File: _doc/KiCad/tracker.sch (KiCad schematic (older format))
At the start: 14 parts

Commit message: Doc
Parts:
- removed Q?: 2N3906, Package_TO_SOT_THT:TO-92_Inline, symbol Transistor_BJT:2N3906
- added Q?: AO3401A, Package_TO_SOT_SMD:SOT-23, symbol Transistor_FET:AO3401A
- D? (x2): value D -> 1N5819
- R?: value 330 -> 10k
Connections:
- net labels removed: GND
- wire segments 43 -> 46
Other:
- moved on the sheet: BT?, C?, D?, J?, R?, U?

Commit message: Doc: schematic
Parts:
- R?: value 3k3 -> 6k8
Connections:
- net at U?.~ (VB): now also D?.1 (K)
- net at U?.~ (VCC): no longer U?.~ (VB)
- net at U?.~ (VB), U?.~ (VCC): now also D?.1 (K)
- new net: U?.~ (VB), U?.~ (VCC) (x4)
- now unconnected: U?.~ (VCC)
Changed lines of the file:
@@
 U 1 1 5FBB3C61
 P 5000 3550
-F 0 "U?" H 5000 4765 50  0000 C CNN
+F 0 "U?" H 5000 4765 50  0001 C CNN
 F 1 "STM32F401 BlackPill" H 5000 4674 50  0000 C CNN
 F 2 "" H 5100 4650 50  0001 C CNN
@@
 U 1 1 5FBB5448
 P 7100 3750
-F 0 "U?" H 7378 3796 50  0000 L CNN
-F 1 "SIM800L" H 7378 3705 50  0000 L CNN
+F 0 "U?" H 7378 3796 50  0001 L CNN
+F 1 "SIM800L" H 7400 3750 50  0000 L CNN
 F 2 "" H 7100 4150 50  0001 C CNN
 F 3 "" H 7100 4150 50  0001 C CNN
@@
 U 1 1 5FBC7BFE
 P 5600 2850
-F 0 "R?" H 5450 2800 50  0000 C CNN
-F 1 "3k3" H 5450 2900 50  0000 C CNN
+F 0 "R?" H 5450 2800 50  0001 C CNN
+F 1 "6k8" H 5450 2850 50  0000 C CNN
 F 2 "" V 5530 2850 50  0001 C CNN
 F 3 "~" H 5600 2850 50  0001 C CNN
@@
 U 1 1 5FBC947C
 P 6300 4650
-F 0 "C?" H 6550 4700 50  0000 C CNN
+F 0 "C?" H 6550 4700 50  0001 C CNN
 F 1 "470mF" H 6550 4600 50  0000 C CNN
 F 2 "" H 6338 4500 50  0001 C CNN
@@
 U 1 1 5FBCCE2D
 P 3650 3850
-F 0 "U?" H 3650 3500 50  0000 C CNN
-F 1 "OLED_SSD1306" H 3650 3400 50  0000 C CNN
+F 0 "U?" H 3650 3500 50  0001 C CNN
+F 1 "OLED_SSD1306" H 3650 3450 50  0000 C CNN
 F 2 "" H 3650 4250 50  0001 C CNN
 F 3 "" H 3650 4250 50  0001 C CNN
@@
 	4150 3400 4150 3800
 Connection ~ 4150 3800
-$Comp
-L Device:R R?
-U 1 1 5FBD5AD0
-P 6350 3450
-F 0 "R?" H 6420 3496 50  0000 L CNN
-F 1 "10" H 6420 3405 50  0000 L CNN
-F 2 "" V 6280 3450 50  0001 C CNN
-F 3 "~" H 6350 3450 50  0001 C CNN
-	1    6350 3450
-	1    0    0    -1
-$EndComp
 Wire Wire Line
 	4150 4400 4150 4800
@@
 U 1 1 5FBD92D9
 P 5750 4700
-F 0 "BT?" H 6000 4800 50  0000 C CNN
+F 0 "BT?" H 6000 4800 50  0001 C CNN
 F 1 "250mAh" H 6000 4700 50  0000 C CNN
 F 2 "" V 5750 4760 50  0001 C CNN
@@
 U 1 1 5FC2FAC7
 P 5850 3100
-F 0 "D?" H 5700 2950 50  0000 C CNN
-F 1 "LED" H 5700 2850 50  0000 C CNN
+F 0 "D?" H 5700 2950 50  0001 C CNN
+F 1 "LED" H 5700 2900 50  0000 C CNN
 F 2 "" H 5850 3100 50  0001 C CNN
 F 3 "~" H 5850 3100 50  0001 C CNN
@@
 U 1 1 5FBC87D2
 P 5600 4250
-F 0 "R?" H 5750 4300 50  0000 C CNN
-F 1 "10k" H 5750 4200 50  0000 C CNN
+F 0 "R?" H 5750 4300 50  0001 C CNN
+F 1 "10k" H 5750 4250 50  0000 C CNN
 F 2 "" V 5530 4250 50  0001 C CNN
 F 3 "~" H 5600 4250 50  0001 C CNN
@@
 U 1 1 5FC34600
 P 6600 2850
-F 0 "D?" V 6554 2930 50  0000 L CNN
-F 1 "1N5819" V 6645 2930 50  0000 L CNN
+F 0 "D?" V 6554 2930 50  0001 L CNN
+F 1 "1N5819" V 6600 2950 50  0000 L CNN
 F 2 "" H 6600 2850 50  0001 C CNN
 F 3 "~" H 6600 2850 50  0001 C CNN
@@
 U 1 1 5FC1A3F2
 P 6000 2850
-F 0 "R?" H 5850 2800 50  0000 C CNN
-F 1 "10k" H 5850 2900 50  0000 C CNN
+F 0 "R?" H 5850 2800 50  0001 C CNN
+F 1 "10k" H 5850 2850 50  0000 C CNN
 F 2 "" V 5930 2850 50  0001 C CNN
 F 3 "~" H 6000 2850 50  0001 C CNN
@@
 U 1 1 60218619
 P 6250 3100
-F 0 "Q?" H 6000 3250 50  0000 L CNN
-F 1 "AO3401A" H 5950 3350 50  0000 L CNN
+F 0 "Q?" H 6000 3250 50  0001 L CNN
+F 1 "AO3401A" H 5900 3300 50  0000 L CNN
 F 2 "Package_TO_SOT_SMD:SOT-23" H 6450 3025 50  0001 L CIN
 F 3 "http://www.aosmd.com/pdfs/datasheet/AO3401A.pdf" H 6250 3100 50  0001 L CNN
@@
 U 1 1 5FBCF7C1
 P 3850 3200
-F 0 "J?" H 3950 3550 50  0000 C CNN
+F 0 "J?" H 3950 3550 50  0001 C CNN
 F 1 "FC UART" H 3950 3450 50  0000 C CNN
 F 2 "" H 3850 3200 50  0001 C CNN
@@
 U 1 1 5FC14E46
 P 4250 3450
-F 0 "D?" V 4350 3400 50  0000 R CNN
+F 0 "D?" V 4350 3400 50  0001 R CNN
 F 1 "1N5819" V 4250 3400 50  0000 R CNN
 F 2 "" H 4250 3450 50  0001 C CNN
@@
 	0    -1   -1   0
 $EndComp
+$Comp
+L Device:R R?
+U 1 1 5FBD5AD0
+P 6350 3450
+F 0 "R?" H 6420 3496 50  0001 L CNN
+F 1 "10" H 6476 3450 50  0000 C CNN
+F 2 "" V 6280 3450 50  0001 C CNN
+F 3 "~" H 6350 3450 50  0001 C CNN
+	1    6350 3450
+	1    0    0    -1
+$EndComp
 $EndSCHEMATC

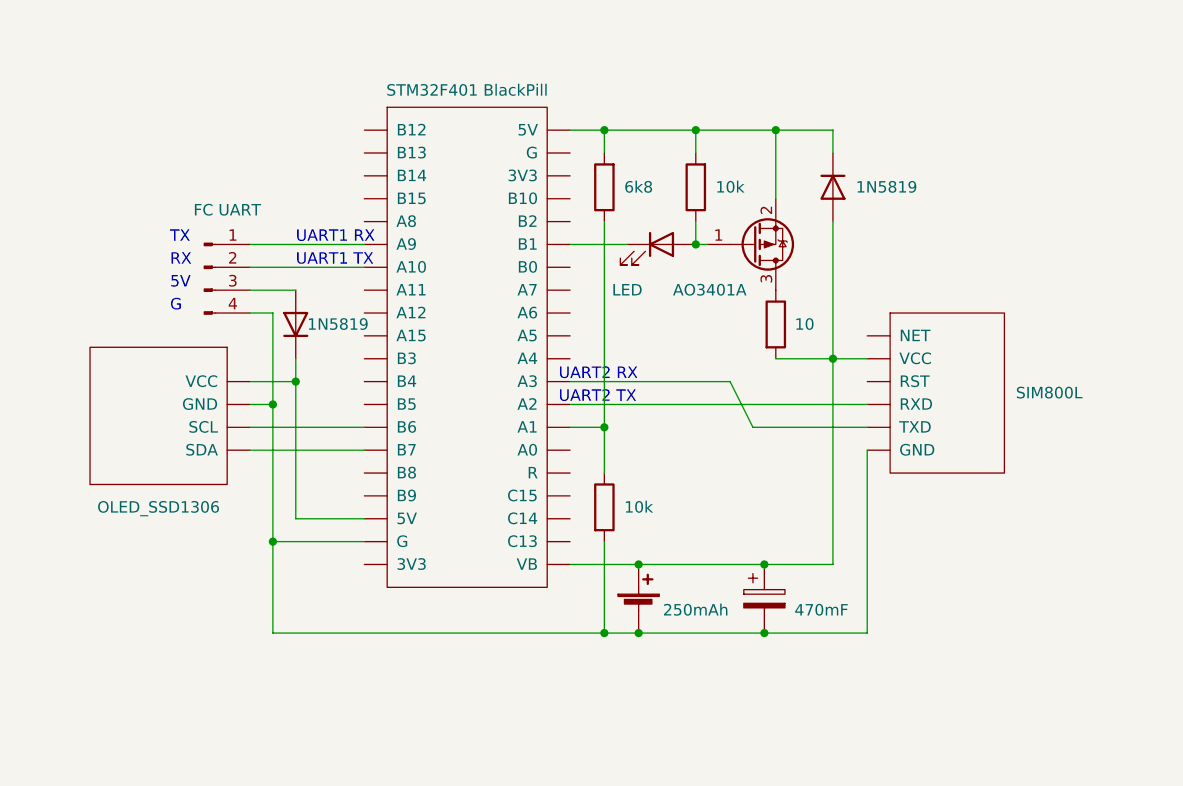
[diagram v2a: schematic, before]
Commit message: Doc: schematic - match current code
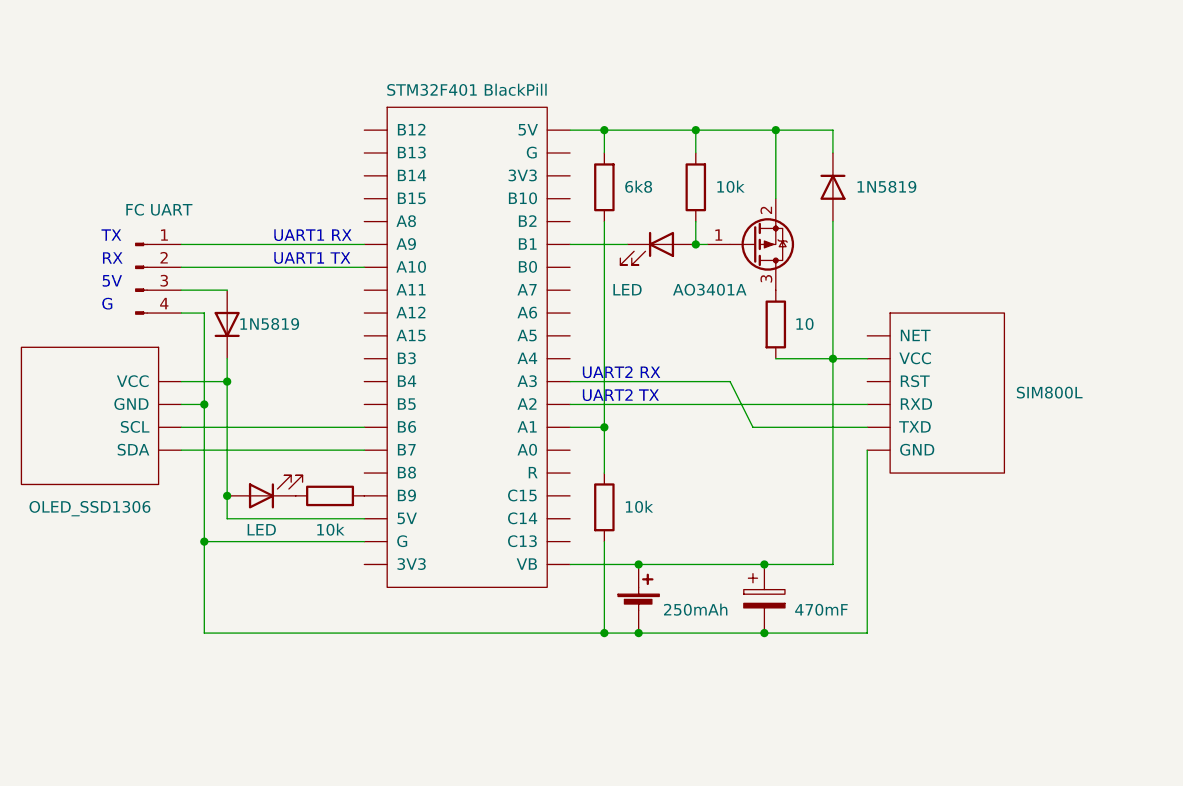
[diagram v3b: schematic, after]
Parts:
- added D?: LED, symbol Device:LED
- added R?: 10k, symbol Device:R
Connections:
- net at U?.~ (VB): now also R?.2
- net at U?.~ (VCC): no longer U?.~ (VB)
- net at U?.~ (VB), U?.~ (VCC): now also D?.1 (K), D?.2 (A)
- new net: U?.~ (VB), U?.~ (VCC) (x4)
- new net: D?.1 (K), R?.1
- now unconnected: U?.~ (VCC)
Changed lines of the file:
@@
 $EndDescr
-$Comp
-L myLib:BlackPill U?
-U 1 1 5FBB3C61
-P 5000 3550
-F 0 "U?" H 5000 4765 50  0001 C CNN
-F 1 "STM32F401 BlackPill" H 5000 4674 50  0000 C CNN
-F 2 "" H 5100 4650 50  0001 C CNN
-F 3 "" H 5100 4650 50  0001 C CNN
-	1    5000 3550
-	1    0    0    -1
-$EndComp
 $Comp
 L myLib:SIM800L U?
@@
 $EndComp
 Wire Wire Line
-	4150 4400 4550 4400
-Wire Wire Line
-	4250 3700 4250 4300
-Wire Wire Line
-	4250 4300 4550 4300
-Wire Wire Line
-	4150 3800 4150 4400
-Wire Wire Line
-	4050 3700 4250 3700
-Wire Wire Line
-	4550 4000 4050 4000
-Wire Wire Line
-	4050 3900 4550 3900
-Wire Wire Line
-	4050 3800 4150 3800
-$Comp
-L myLib:OLED_SSD1306 U?
-U 1 1 5FBCCE2D
-P 3650 3850
-F 0 "U?" H 3650 3500 50  0001 C CNN
-F 1 "OLED_SSD1306" H 3650 3450 50  0000 C CNN
-F 2 "" H 3650 4250 50  0001 C CNN
-F 3 "" H 3650 4250 50  0001 C CNN
-	1    3650 3850
-	1    0    0    -1
-$EndComp
-Connection ~ 4250 3700
-Wire Wire Line
-	4150 3400 4150 3800
-Connection ~ 4150 3800
-Wire Wire Line
-	4150 4400 4150 4800
-Connection ~ 4150 4400
+	3850 4400 4550 4400
+Wire Wire Line
+	3950 3700 3950 4200
+Wire Wire Line
+	3950 4300 4550 4300
+Wire Wire Line
+	3850 3800 3850 4400
+Connection ~ 3950 3700
+Wire Wire Line
+	3850 3400 3850 3800
+Connection ~ 3850 3800
+Wire Wire Line
+	3850 4400 3850 4800
+Connection ~ 3850 4400
 Wire Wire Line
 	5450 3700 6150 3700
 Wire Wire Line
-	4250 3600 4250 3700
+	3950 3600 3950 3700
 $Comp
 L Device:Battery_Cell BT?
@@
 $EndComp
 Wire Wire Line
-	4150 4800 5600 4800
+	3850 4800 5600 4800
 Connection ~ 5750 4500
 Wire Wire Line
@@
 	1    0    0    -1
 $EndComp
-Text Notes 4250 3200 0    50   ~ 0
+Text Notes 4150 3200 0    50   ~ 0
 UART1 TX
-Text Notes 4250 3100 0    50   ~ 0
+Text Notes 4150 3100 0    50   ~ 0
 UART1 RX\n
 Wire Wire Line
@@
 Wire Wire Line
 	5750 4500 6300 4500
-Text Notes 3700 3100 0    50   ~ 0
+Text Notes 3400 3100 0    50   ~ 0
 TX
-Text Notes 3700 3200 0    50   ~ 0
+Text Notes 3400 3200 0    50   ~ 0
 RX
-Text Notes 3700 3300 0    50   ~ 0
+Text Notes 3400 3300 0    50   ~ 0
 5V
-Text Notes 3700 3400 0    50   ~ 0
+Text Notes 3400 3400 0    50   ~ 0
 G
 Connection ~ 6350 2600
@@
 	6000 3100 6050 3100
 Connection ~ 6000 3100
-Text Notes 5400 3800 0    50   ~ 0
+Text Notes 5500 3800 0    50   ~ 0
 UART2 TX
-Text Notes 5400 3700 0    50   ~ 0
+Text Notes 5500 3700 0    50   ~ 0
 UART2 RX\n
-Wire Wire Line
-	4050 3400 4150 3400
-Wire Wire Line
-	4050 3300 4250 3300
-Wire Wire Line
-	4550 3200 4050 3200
-Wire Wire Line
-	4050 3100 4550 3100
-$Comp
-L Connector:Conn_01x04_Male J?
-U 1 1 5FBCF7C1
-P 3850 3200
-F 0 "J?" H 3950 3550 50  0001 C CNN
-F 1 "FC UART" H 3950 3450 50  0000 C CNN
-F 2 "" H 3850 3200 50  0001 C CNN
-F 3 "~" H 3850 3200 50  0001 C CNN
-	1    3850 3200
-	1    0    0    -1
-$EndComp
 $Comp
 L Device:D D?
 U 1 1 5FC14E46
-P 4250 3450
-F 0 "D?" V 4350 3400 50  0001 R CNN
-F 1 "1N5819" V 4250 3400 50  0000 R CNN
-F 2 "" H 4250 3450 50  0001 C CNN
-F 3 "~" H 4250 3450 50  0001 C CNN
-	1    4250 3450
+P 3950 3450
+F 0 "D?" V 4050 3400 50  0001 R CNN
+F 1 "1N5819" V 3950 3400 50  0000 R CNN
+F 2 "" H 3950 3450 50  0001 C CNN
+F 3 "~" H 3950 3450 50  0001 C CNN
+	1    3950 3450
 	0    -1   -1   0
 $EndComp
@@
 	1    0    0    -1
 $EndComp
+$Comp
+L myLib:OLED_SSD1306 U?
+U 1 1 5FBCCE2D
+P 3350 3850
+F 0 "U?" H 3350 3500 50  0001 C CNN
+F 1 "OLED_SSD1306" H 3350 3450 50  0000 C CNN
+F 2 "" H 3350 4250 50  0001 C CNN
+F 3 "" H 3350 4250 50  0001 C CNN
+	1    3350 3850
+	1    0    0    -1
+$EndComp
+Wire Wire Line
+	3750 3800 3850 3800
+Wire Wire Line
+	3750 3900 4550 3900
+Wire Wire Line
+	4550 4000 3750 4000
+Wire Wire Line
+	3750 3700 3950 3700
+Wire Wire Line
+	3750 3400 3850 3400
+Wire Wire Line
+	3750 3300 3950 3300
+Wire Wire Line
+	4550 3200 3750 3200
+Wire Wire Line
+	3750 3100 4550 3100
+$Comp
+L Connector:Conn_01x04_Male J?
+U 1 1 5FBCF7C1
+P 3550 3200
+F 0 "J?" H 3650 3550 50  0001 C CNN
+F 1 "FC UART" H 3650 3450 50  0000 C CNN
+F 2 "" H 3550 3200 50  0001 C CNN
+F 3 "~" H 3550 3200 50  0001 C CNN
+	1    3550 3200
+	1    0    0    -1
+$EndComp
+$Comp
+L Device:R R?
+U 1 1 61E34BAE
+P 4400 4200
+F 0 "R?" H 4250 4150 50  0001 C CNN
+F 1 "10k" V 4250 4200 50  0000 C CNN
+F 2 "" V 4330 4200 50  0001 C CNN
+F 3 "~" H 4400 4200 50  0001 C CNN
+	1    4400 4200
+	0    -1   -1   0
+$EndComp
+$Comp
+L Device:LED D?
+U 1 1 61E372F0
+P 4100 4200
+F 0 "D?" H 3950 4050 50  0001 C CNN
+F 1 "LED" H 4100 4350 50  0000 C CNN
+F 2 "" H 4100 4200 50  0001 C CNN
+F 3 "~" H 4100 4200 50  0001 C CNN
+	1    4100 4200
+	-1   0    0    1
+$EndComp
+Connection ~ 3950 4200
+Wire Wire Line
+	3950 4200 3950 4300
+$Comp
+L myLib:BlackPill U?
+U 1 1 5FBB3C61
+P 5000 3550
+F 0 "U?" H 5000 4765 50  0001 C CNN
+F 1 "STM32F401 BlackPill" H 5000 4674 50  0000 C CNN
+F 2 "" H 5100 4650 50  0001 C CNN
+F 3 "" H 5100 4650 50  0001 C CNN
+	1    5000 3550
+	1    0    0    -1
+$EndComp

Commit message: Doc: schematic
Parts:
- added D?: GREEN, symbol Device:LED
- added D?: RED, symbol Device:LED
- added R? (x2): 3k3, symbol Device:R
- D?: value LED -> BLUE
- R?: value 10k -> 3k3
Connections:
- net at U?.~ (VB): now also R?.2
- net at U?.~ (VCC): no longer U?.~ (VB)
- net at U?.~ (VB), U?.~ (VCC): now also D?.1 (K)
- net at J?.1 (Pin_1), U?.~ (VB): now also BT?.2 (-), C?.2, D?.1 (K), R?.2, U?.~ (VCC), U?.~ (VCC), D?.1 (K), D?.1 (K)
- net at J?.2 (Pin_2): now also D?.2 (A); no longer U?.~ (VB)
- net at J?.3 (Pin_3): now also U?.~ (VB); no longer D?.2 (A)
- net at R?.1: now also D?.2 (A); no longer D?.1 (K)
- new net: U?.~ (VB), U?.~ (VCC) (x4)
- new net: J?.4 (Pin_4), U?.~ (VB)
- new net: R?.2, U?.~ (VB) (x2)
- new net: D?.2 (A), R?.1 (x2)
- now unconnected: U?.~ (VCC), U?.~ (VCC)
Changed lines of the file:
@@
 P 7100 3750
 F 0 "U?" H 7378 3796 50  0001 L CNN
-F 1 "SIM800L" H 7400 3750 50  0000 L CNN
+F 1 "SIM800L" H 6950 3300 50  0000 L CNN
 F 2 "" H 7100 4150 50  0001 C CNN
 F 3 "" H 7100 4150 50  0001 C CNN
@@
 $EndComp
 Wire Wire Line
-	3850 4400 4550 4400
-Wire Wire Line
-	3950 3700 3950 4200
-Wire Wire Line
-	3950 4300 4550 4300
-Wire Wire Line
-	3850 3800 3850 4400
-Connection ~ 3950 3700
-Wire Wire Line
-	3850 3400 3850 3800
-Connection ~ 3850 3800
-Wire Wire Line
-	3850 4400 3850 4800
-Connection ~ 3850 4400
+	3950 4400 4550 4400
+Wire Wire Line
+	4050 4300 4550 4300
+Wire Wire Line
+	3950 3800 3950 4400
+Connection ~ 4050 3700
+Connection ~ 3950 3800
+Wire Wire Line
+	3950 4400 3950 4800
+Connection ~ 3950 4400
 Wire Wire Line
 	5450 3700 6150 3700
 Wire Wire Line
-	3950 3600 3950 3700
+	4050 3600 4050 3700
 $Comp
 L Device:Battery_Cell BT?
@@
 $EndComp
 Wire Wire Line
-	3850 4800 5600 4800
+	3950 4800 5600 4800
 Connection ~ 5750 4500
 Wire Wire Line
@@
 Text Notes 3400 3200 0    50   ~ 0
 RX
-Text Notes 3400 3300 0    50   ~ 0
+Text Notes 3400 3000 0    50   ~ 0
 5V
-Text Notes 3400 3400 0    50   ~ 0
-G
 Connection ~ 6350 2600
 Wire Wire Line
@@
 L Device:D D?
 U 1 1 5FC14E46
-P 3950 3450
-F 0 "D?" V 4050 3400 50  0001 R CNN
-F 1 "1N5819" V 3950 3400 50  0000 R CNN
-F 2 "" H 3950 3450 50  0001 C CNN
-F 3 "~" H 3950 3450 50  0001 C CNN
-	1    3950 3450
+P 4050 3450
+F 0 "D?" V 4150 3400 50  0001 R CNN
+F 1 "1N5819" V 4050 3400 50  0000 R CNN
+F 2 "" H 4050 3450 50  0001 C CNN
+F 3 "~" H 4050 3450 50  0001 C CNN
+	1    4050 3450
 	0    -1   -1   0
 $EndComp
@@
 L myLib:OLED_SSD1306 U?
 U 1 1 5FBCCE2D
-P 3350 3850
-F 0 "U?" H 3350 3500 50  0001 C CNN
-F 1 "OLED_SSD1306" H 3350 3450 50  0000 C CNN
-F 2 "" H 3350 4250 50  0001 C CNN
-F 3 "" H 3350 4250 50  0001 C CNN
-	1    3350 3850
-	1    0    0    -1
-$EndComp
-Wire Wire Line
-	3750 3800 3850 3800
-Wire Wire Line
-	3750 3900 4550 3900
-Wire Wire Line
-	4550 4000 3750 4000
-Wire Wire Line
-	3750 3700 3950 3700
-Wire Wire Line
-	3750 3400 3850 3400
-Wire Wire Line
-	3750 3300 3950 3300
+P 3500 3850
+F 0 "U?" H 3500 3500 50  0001 C CNN
+F 1 "OLED_SSD1306" H 3500 3450 50  0000 C CNN
+F 2 "" H 3500 4250 50  0001 C CNN
+F 3 "" H 3500 4250 50  0001 C CNN
+	1    3500 3850
+	1    0    0    -1
+$EndComp
+Wire Wire Line
+	3900 3800 3950 3800
+Wire Wire Line
+	3900 3900 4550 3900
+Wire Wire Line
+	4550 4000 3900 4000
+Wire Wire Line
+	3900 3700 4050 3700
 Wire Wire Line
 	4550 3200 3750 3200
@@
 L Connector:Conn_01x04_Male J?
 U 1 1 5FBCF7C1
-P 3550 3200
-F 0 "J?" H 3650 3550 50  0001 C CNN
-F 1 "FC UART" H 3650 3450 50  0000 C CNN
-F 2 "" H 3550 3200 50  0001 C CNN
-F 3 "~" H 3550 3200 50  0001 C CNN
-	1    3550 3200
-	1    0    0    -1
-$EndComp
-$Comp
-L Device:R R?
-U 1 1 61E34BAE
-P 4400 4200
-F 0 "R?" H 4250 4150 50  0001 C CNN
-F 1 "10k" V 4250 4200 50  0000 C CNN
-F 2 "" V 4330 4200 50  0001 C CNN
-F 3 "~" H 4400 4200 50  0001 C CNN
-	1    4400 4200
-	0    -1   -1   0
-$EndComp
-$Comp
-L Device:LED D?
-U 1 1 61E372F0
-P 4100 4200
-F 0 "D?" H 3950 4050 50  0001 C CNN
-F 1 "LED" H 4100 4350 50  0000 C CNN
-F 2 "" H 4100 4200 50  0001 C CNN
-F 3 "~" H 4100 4200 50  0001 C CNN
-	1    4100 4200
-	-1   0    0    1
-$EndComp
-Connection ~ 3950 4200
-Wire Wire Line
-	3950 4200 3950 4300
+P 3550 3000
+F 0 "J?" H 3650 3350 50  0001 C CNN
+F 1 "FC UART" H 3550 2700 50  0000 C CNN
+F 2 "" H 3550 3000 50  0001 C CNN
+F 3 "~" H 3550 3000 50  0001 C CNN
+	1    3550 3000
+	1    0    0    -1
+$EndComp
 $Comp
 L myLib:BlackPill U?
@@
 P 5000 3550
 F 0 "U?" H 5000 4765 50  0001 C CNN
-F 1 "STM32F401 BlackPill" H 5000 4674 50  0000 C CNN
+F 1 "STM32F401 BlackPill" H 5000 2400 50  0000 C CNN
 F 2 "" H 5100 4650 50  0001 C CNN
 F 3 "" H 5100 4650 50  0001 C CNN
@@
 	1    0    0    -1
 $EndComp
+Wire Wire Line
+	4050 3700 4050 4300
+Text Notes 3400 2900 0    50   ~ 0
+G
+$Comp
+L Device:R R?
+U 1 1 61E2F3F9
+P 4400 2800
+F 0 "R?" H 4250 2750 50  0001 C CNN
+F 1 "3k3" V 4400 2800 50  0000 C CNN
+F 2 "" V 4330 2800 50  0001 C CNN
+F 3 "~" H 4400 2800 50  0001 C CNN
+	1    4400 2800
+	0    -1   -1   0
+$EndComp
+$Comp
+L Device:R R?
+U 1 1 61E2F33D
+P 4400 2700
+F 0 "R?" H 4250 2650 50  0001 C CNN
+F 1 "3k3" V 4400 2700 50  0000 C CNN
+F 2 "" V 4330 2700 50  0001 C CNN
+F 3 "~" H 4400 2700 50  0001 C CNN
+	1    4400 2700
+	0    -1   -1   0
+$EndComp
+$Comp
+L Device:R R?
+U 1 1 61E34BAE
+P 4400 2600
+F 0 "R?" H 4250 2550 50  0001 C CNN
+F 1 "3k3" V 4400 2600 50  0000 C CNN
+F 2 "" V 4330 2600 50  0001 C CNN
+F 3 "~" H 4400 2600 50  0001 C CNN
+	1    4400 2600
+	0    -1   -1   0
+$EndComp
+$Comp
+L Device:LED D?
+U 1 1 61E2F53B
+P 4100 2800
+F 0 "D?" H 3950 2650 50  0001 C CNN
+F 1 "RED" H 3850 2850 50  0000 R CNN
+F 2 "" H 4100 2800 50  0001 C CNN
+F 3 "~" H 4100 2800 50  0001 C CNN
+	1    4100 2800
+	1    0    0    -1
+$EndComp
+Wire Wire Line
+	3950 2600 3950 2700
+$Comp
+L Device:LED D?
+U 1 1 61E2F4B0
+P 4100 2700
+F 0 "D?" H 3950 2550 50  0001 C CNN
+F 1 "GREEN" H 3850 2750 50  0000 R CNN
+F 2 "" H 4100 2700 50  0001 C CNN
+F 3 "~" H 4100 2700 50  0001 C CNN
+	1    4100 2700
+	1    0    0    -1
+$EndComp
+$Comp
+L Device:LED D?
+U 1 1 61E372F0
+P 4100 2600
+F 0 "D?" H 3950 2450 50  0001 C CNN
+F 1 "BLUE" H 3850 2650 50  0000 R CNN
+F 2 "" H 4100 2600 50  0001 C CNN
+F 3 "~" H 4100 2600 50  0001 C CNN
+	1    4100 2600
+	1    0    0    -1
+$EndComp
+Connection ~ 3950 2700
+Wire Wire Line
+	3950 2700 3950 2800
+Connection ~ 3950 2800
+Wire Wire Line
+	3950 2800 3950 2900
+Wire Wire Line
+	3750 2900 3950 2900
+Connection ~ 3950 2900
+Wire Wire Line
+	3950 2900 3950 3800
+Wire Wire Line
+	3750 3000 4050 3000
+Wire Wire Line
+	4050 3000 4050 3300
 $EndSCHEMATC
